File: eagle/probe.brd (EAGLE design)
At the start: 21.8 x 21.8 mm, 11 parts

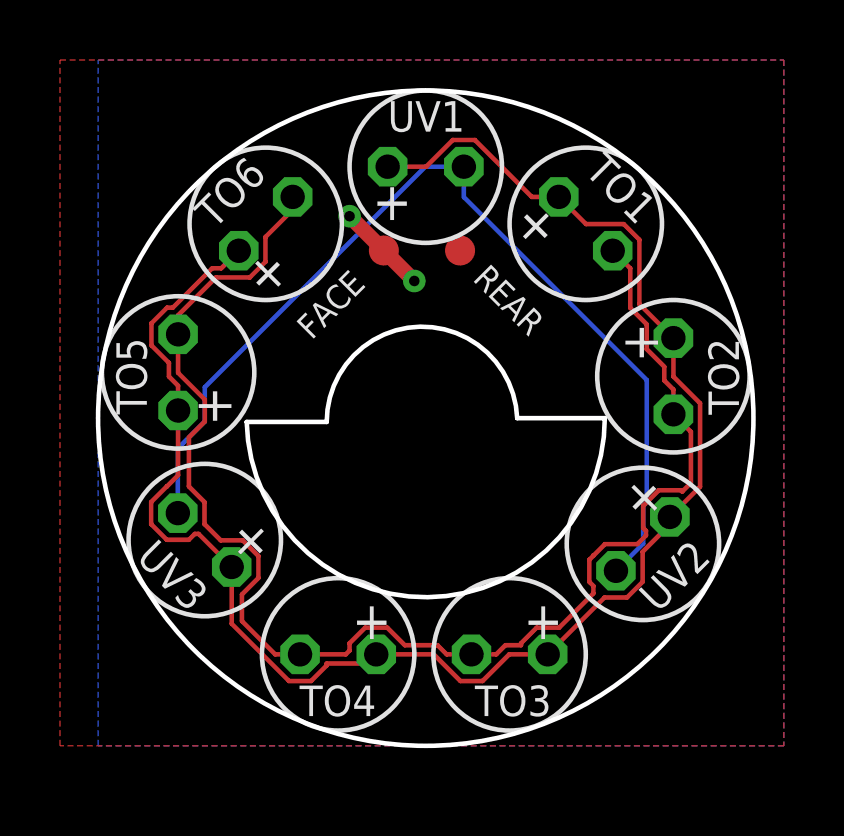
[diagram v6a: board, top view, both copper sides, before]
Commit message: Re-organise eagle folder
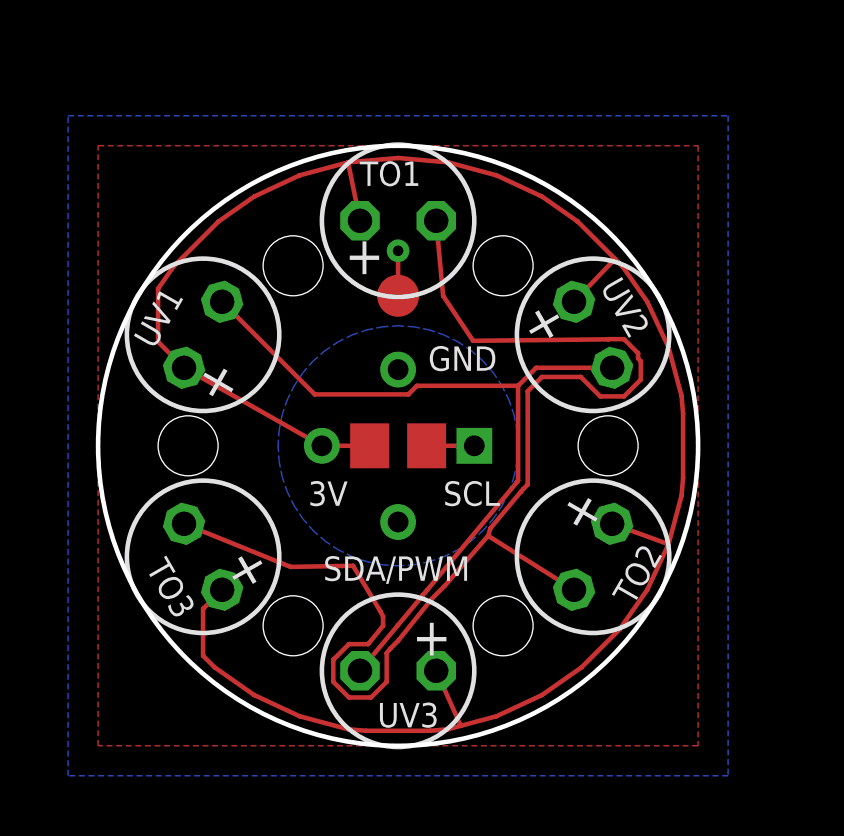
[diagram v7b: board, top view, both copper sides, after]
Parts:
- removed REAR: TPTP10R, testpad:TP10R
- removed TO4, TO5, TO6: (no value), general:LED5MM
- added R1: 10k, resistor:R0805
- added U1: MLX90614ESF-BAA-000-TU, MLX90614ESF-BAA-000-TU:TO254P942H425-4
- FACE: value TPTP10R -> TPTP14R; device testpad:TP10R -> testpad:TP14R
- moved TO3 10.7 mm to (3.50, 6.30), turned to 120 degrees
- moved UV1 9.30 mm to (3.50, 13.7), turned to 60 degrees
- moved UV3 7.78 mm to (10.0, 2.50), turned to 180 degrees
- moved UV2 7.16 mm to (16.5, 13.7), turned to 300 degrees
- moved TO2 6.59 mm to (16.5, 6.30), turned to 240 degrees
- moved TO1 6.26 mm to (10.0, 17.5), turned to 0 degrees
- moved FACE 1.58 mm to (10.0, 15.0)
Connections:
- removed net N$1: TO1.A, TO2.A, TO3.A, TO4.A, TO5.A, TO6.A, UV1.A, UV2.A, UV3.A
- removed net REAR: REAR.TP
- new net 3V: R1.2, TO1.A, TO2.A, TO3.A, U1.3, UV1.A, UV2.A, UV3.A
- new net GND: U1.4
- new net SCL: R1.1, U1.1
- net N$2: no longer TO4.K, TO5.K, TO6.K
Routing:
- net 3V: track 0.00 -> 67.0 mm
- net N$1: track 56.5 -> 0.00 mm
- net N$4: track 32.7 -> 26.1 mm
- net N$2: track 47.7 -> 43.5 mm
- net SCL: track 0.00 -> 1.59 mm
- net FACE: track 3.05 -> 1.50 mm, vias 2 -> 1
- added copper zone on layer 1, net GND
- added copper zone on layer 16, net GND
- removed copper zone on layer 1, net REAR
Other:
- board size 21.8 x 21.8 mm -> 20 x 20 mm
- board text added: "3V"
- board text added: "GND"
- board text added: "SCL"
- board text added: "SDA/PWM"

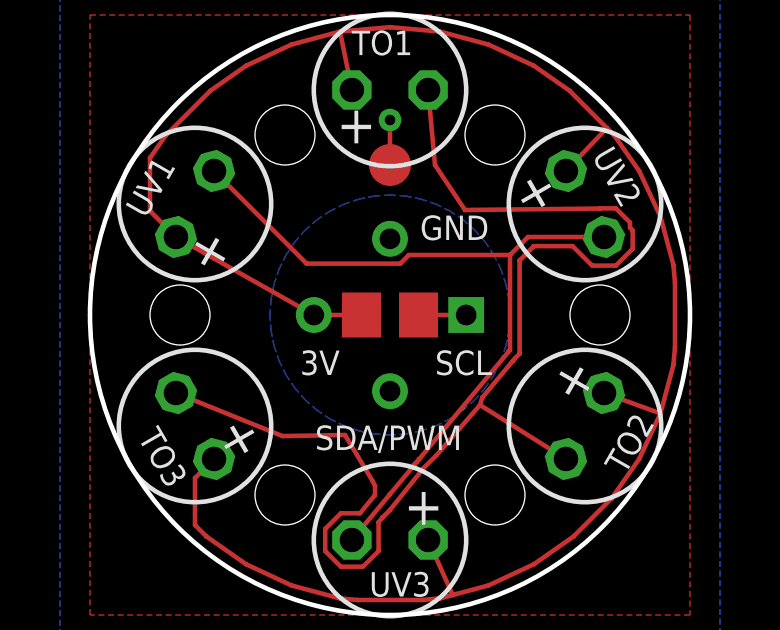
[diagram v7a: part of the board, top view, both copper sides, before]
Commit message: First order of probe, probebase and FFC breakout PCBs for 22mm enclosure
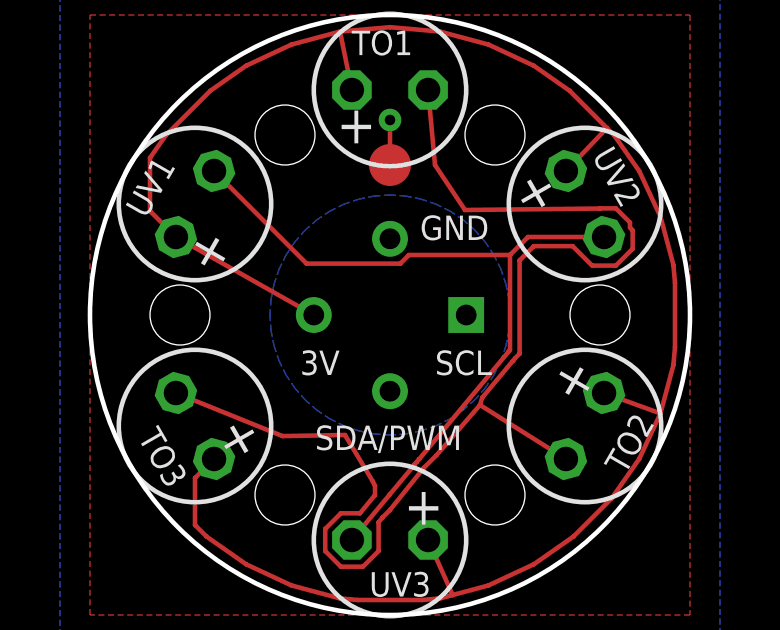
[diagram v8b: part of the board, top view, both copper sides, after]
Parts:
- removed R1: 10k, resistor:R0805
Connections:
- removed net SCL: R1.1, U1.1
- net 3V: no longer R1.2
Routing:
- net 3V: track 67.0 -> 65.4 mm
- net SCL: track 1.59 -> 0.00 mm
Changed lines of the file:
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@@
 <attribute name="VALUE" x="9.492" y="14.238" size="0.0254" layer="27"/>
-</element>
-<element name="R1" library="resistor" library_urn="urn:adsk.eagle:library:348" package="R0805" package3d_urn="urn:adsk.eagle:package:23553/2" value="10k" x="10" y="10" smashed="yes" rot="R180">
-<attribute name="VALUE" x="10.635" y="12.54" size="1.27" layer="27" rot="R180"/>
 </element>
 </elements>
@@
 <wire x1="17.135" y1="7.39985" x2="19.015034375" y2="6.718796875" width="0.1524" layer="1"/>
 <wire x1="11.27" y1="2.5" x2="12.08958125" y2="0.665671875" width="0.1524" layer="1"/>
-<contactref element="R1" pad="2"/>
-<wire x1="9.05" y1="10" x2="7.46" y2="10" width="0.1524" layer="1"/>
-</signal>
-<signal name="SCL">
-<contactref element="U1" pad="1"/>
-<contactref element="R1" pad="1"/>
-<wire x1="10.95" y1="10" x2="12.54" y2="10" width="0.1524" layer="1"/>
 </signal>
 </signals>
